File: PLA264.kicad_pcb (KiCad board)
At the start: 2 copper layers, 18.3 x 37.1 mm, 9 parts, among them J1 PLA_Socket, U1 GAL16V8

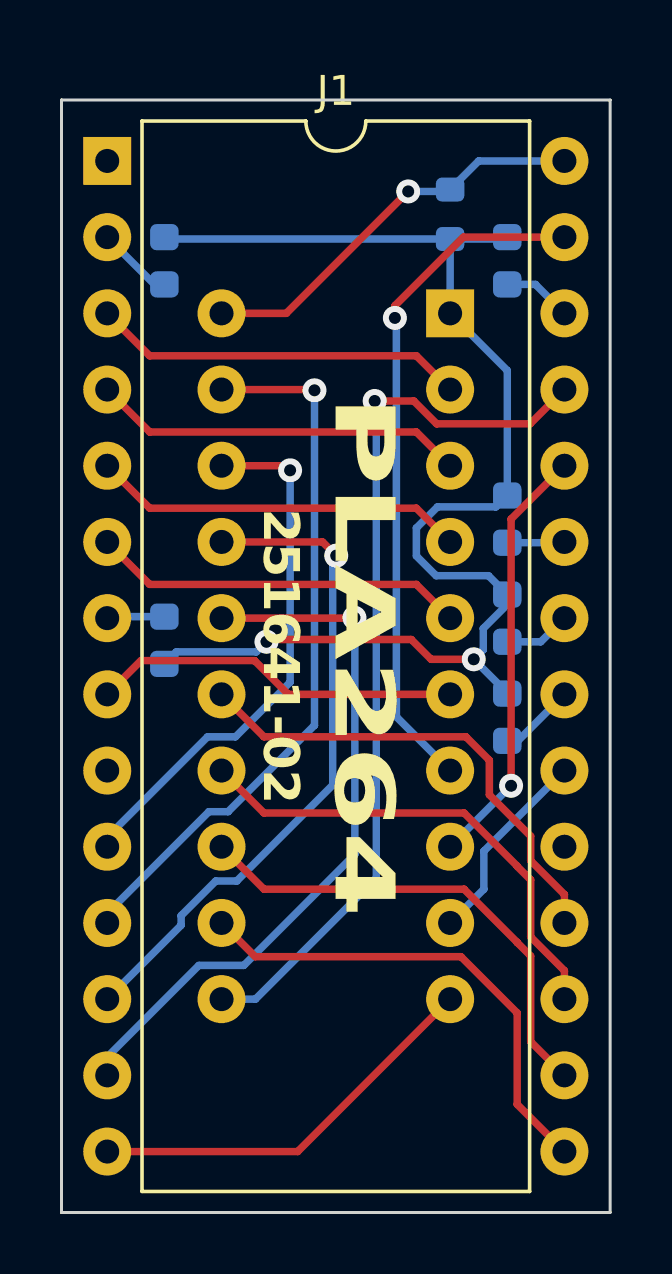
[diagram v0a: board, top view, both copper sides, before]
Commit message: Revised layout.
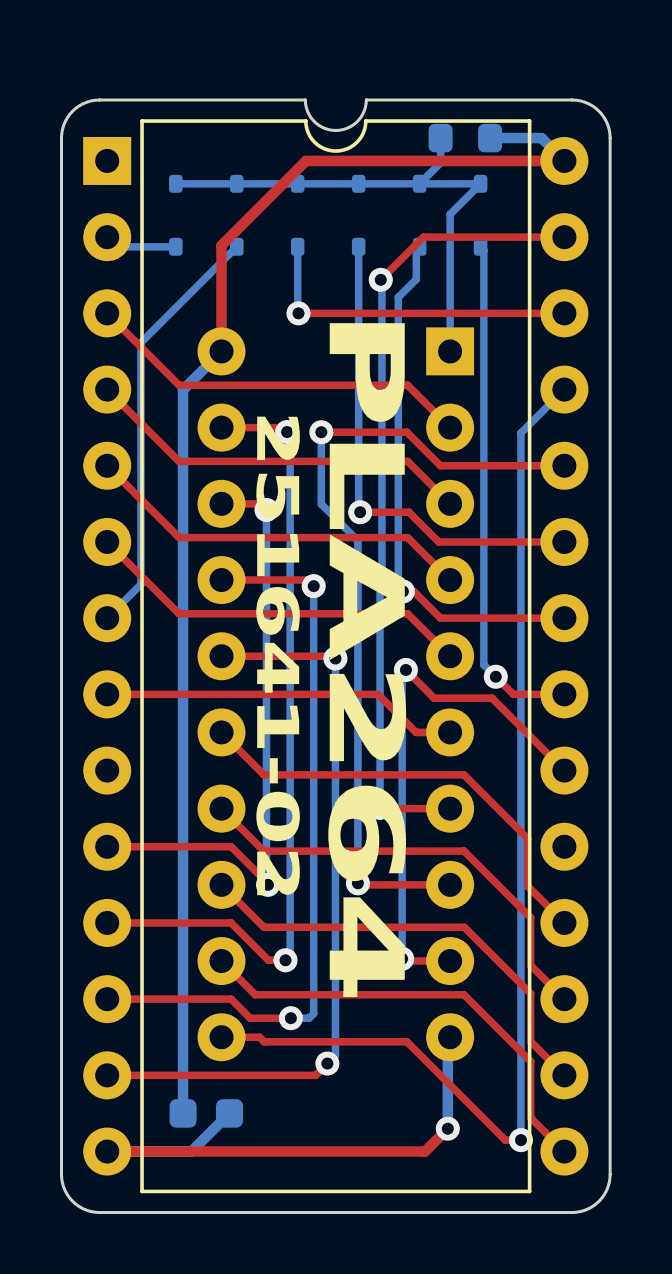
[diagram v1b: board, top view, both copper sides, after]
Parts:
- added C1: 100n, Capacitor_SMD:C_0603_1608Metric, B.Cu at (99.8, 87.6)
- D1, D2, D3, D4, D5, D6: footprint Diode_SMD:D_0603_1608Metric -> Diode_SMD:D_SOD-323
- moved D4 16.8 mm to (109.0, 57.7)
- moved D6 14.4 mm to (100.8, 57.7), turned to 90 degrees
- moved D3 13.7 mm to (106.9, 57.7)
- moved D2 11.3 mm to (104.9, 57.7)
- moved D1 7.15 mm to (102.9, 57.7)
- moved R1 2.59 mm to (108.5, 55.1), turned to 180 degrees
- moved D5 1.56 mm to (98.8, 57.7)
- moved U1 1.27 mm to (108.0, 62.2)
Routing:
- net +5V: track 13.5 -> 44.9 mm, vias 1 -> 0
- net Net-(D1-A): track 43.9 -> 18.0 mm, vias 2 -> 0
- net /A11: track 2.23 -> 17.6 mm, vias 0 -> 1
- net /A10: track 2.55 -> 17.1 mm, vias 0 -> 1
- net /A13: track 1.92 -> 16.1 mm, vias 0 -> 1
- net /A9: track 14.3 -> 27.2 mm, vias 1 -> 2
- net /A15: track 1.93 -> 14.2 mm
- net /RAS: track 6.66 -> 18.0 mm, vias 0 -> 2
- net /A14: track 2.30 -> 11.1 mm, vias 0 -> 1
- net /A8: track 29.9 -> 37.0 mm
- net GND: track 13.5 -> 19.4 mm, vias 0 -> 1
- net /MUX: track 22.9 -> 26.7 mm, vias 1 -> 2
- net /LOOP: track 24.1 -> 26.4 mm, vias 1 -> 2
- net /KB_SPI: track 22.4 -> 24.6 mm, vias 1 -> 2
- net /KERNAL: track 18.0 -> 20.0 mm, vias 1 -> 2
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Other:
- outline, holes or cut-outs redrawn

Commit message: Cleaning up.
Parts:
- D1: renamed from D5; value D_Small -> 1N4148WS
- D2: renamed from D6; value D_Small -> 1N4148WS
- D3: renamed from D1; value D_Small -> 1N4148WS
- D4: renamed from D2; value D_Small -> 1N4148WS
- D5: renamed from D3; value D_Small -> 1N4148WS
- D6: renamed from D4; value D_Small -> 1N4148WS
- moved D1 0.25 mm to (99.1, 57.7)
- moved D2 0.25 mm to (101.1, 57.7)
- moved D4 0.25 mm to (105.2, 57.7)
- moved D5 0.25 mm to (107.2, 57.7)
- moved D6 0.25 mm to (109.2, 57.7)
- moved D3 0.25 mm to (103.1, 57.7)
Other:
- board size 18.3 x 37.1 mm -> 17.8 x 36.6 mm
- board text added: "github.com/hackup/PLA264"

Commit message: Preparing for Gerber export.
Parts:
- added G***: LOGO, Logo:bigby3-cu, F.Cu at (104.1, 88.6)
- R1: value R -> 5k6
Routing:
- net GND: track 19.4 -> 17.6 mm, vias 1 -> 0
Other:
- board text added: "PLA264 Rev.0"
